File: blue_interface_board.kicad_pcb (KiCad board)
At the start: 2 copper layers, 0 parts

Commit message: Added protection from motor regeneration through capacitors + MOSFET, started placement and routing
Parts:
- added C1: 100n, Capacitor_SMD:C_0603_1608Metric, F.Cu at (96.6, 110.0)
- added C10: 27p, Capacitor_SMD:C_0603_1608Metric, F.Cu at (117.6, 120.2)
- added C11: 4.7u, Capacitor_SMD:C_0603_1608Metric, B.Cu at (113.5, 111.0)
- added C12: 100n, Capacitor_SMD:C_0603_1608Metric, B.Cu at (113.5, 112.5)
- added C13: 100n, Capacitor_SMD:C_0603_1608Metric, F.Cu at (108.8, 114.0)
- added C14: 100n, Capacitor_SMD:C_0603_1608Metric, F.Cu at (118.0, 117.0)
- added C15: 4.7u, Capacitor_SMD:C_0603_1608Metric, B.Cu at (116.5, 111.0)
- added C16: 100n, Capacitor_SMD:C_0603_1608Metric, F.Cu at (121.2, 108.5)
- added C17: 100n, Capacitor_SMD:C_0603_1608Metric, B.Cu at (116.5, 112.5)
- added C18: 100n, Capacitor_SMD:C_0603_1608Metric, F.Cu at (124.8, 108.1)
- added C19: 10n, Capacitor_SMD:C_0603_1608Metric, F.Cu at (126.2, 108.1)
- added C2: 4.7u, Capacitor_SMD:C_0603_1608Metric, F.Cu at (107.5, 108.0)
- added C20: 100n, Capacitor_SMD:C_0603_1608Metric, F.Cu at (126.2, 115.8)
- added C21: 10u, Capacitor_SMD:C_0603_1608Metric, F.Cu at (124.8, 115.8)
- added C22: 100n, Capacitor_SMD:C_0603_1608Metric, F.Cu at (142.0, 108.2)
- added C23: 10n, Capacitor_SMD:C_0603_1608Metric, F.Cu at (140.5, 108.2)
- added C24: 100n, Capacitor_SMD:C_0603_1608Metric, F.Cu at (140.5, 115.8)
- added C25: 10u, Capacitor_SMD:C_0603_1608Metric, F.Cu at (142.0, 115.8)
- added C26: 10n, Capacitor_SMD:C_0603_1608Metric, F.Cu at (101.2, 115.0)
- added C27: 150nF, Capacitor_SMD:C_1206_3216Metric, F.Cu at (67.7, 77.5)
- added C28: 100nF, Capacitor_SMD:C_1206_3216Metric, F.Cu at (-96.5, 58.5)
- added C29: 1uF, Capacitor_SMD:C_0603_1608Metric, F.Cu at (87.1, 65.8)
- added C3: 4.7u, Capacitor_SMD:C_0603_1608Metric, B.Cu at (107.5, 108.0)
- added C30: 1uF, Capacitor_SMD:C_0603_1608Metric, F.Cu at (82.6, 70.4)
- added C31: 100n, Capacitor_SMD:C_0603_1608Metric, F.Cu at (113.2, 40.7)
- added C32: 470u, Capacitor_SMD:CP_Elec_18x17.5, F.Cu at (-49.0, 46.0)
- added C33: 470u, Capacitor_SMD:CP_Elec_18x17.5, F.Cu at (-29.0, 46.0)
- added C34: 470u, Capacitor_SMD:CP_Elec_18x17.5, F.Cu at (11.0, 46.0)
- added C35: 470u, Capacitor_SMD:CP_Elec_18x17.5, F.Cu at (-9.00, 46.0)
- added C38: 1u, Capacitor_SMD:C_0603_1608Metric, F.Cu at (47.0, 78.2)
- added C39: 1u, Capacitor_SMD:C_0603_1608Metric, F.Cu at (26.9, 78.2)
- added C4: 100n, Capacitor_SMD:C_0603_1608Metric, B.Cu at (112.8, 107.0)
- added C40: 100n, Capacitor_SMD:C_0603_1608Metric, F.Cu at (-84.0, 40.0)
- added C5: 10n, Capacitor_SMD:C_0603_1608Metric, F.Cu at (114.0, 104.2)
- added C6: 100n, Capacitor_SMD:C_0603_1608Metric, F.Cu at (109.0, 108.0)
- added C7: 100n, Capacitor_SMD:C_0603_1608Metric, B.Cu at (109.0, 108.0)
- added C8: 100n, Capacitor_SMD:C_0603_1608Metric, F.Cu at (110.5, 106.0)
- added C9: 27p, Capacitor_SMD:C_0603_1608Metric, F.Cu at (107.4, 120.2)
- added D1: LED, LED_SMD:LED_0603_1608Metric, F.Cu at (118.5, 99.8)
- added D2: LED, LED_SMD:LED_0603_1608Metric, F.Cu at (116.6, 99.8)
- added D3: 1N4148W-7-F, Diode_SMD:D_SOD-123, F.Cu at (67.8, 74.2)
- added D4: 5.0SMDJ51A, Diode_SMD:D_SMC, F.Cu at (-103.0, 58.5)
- added D5: B380-13-F, Diode_SMD:D_SMC, F.Cu at (-63.5, 56.5)
- added D6: LED, LED_SMD:LED_0603_1608Metric, F.Cu at (22.9, 78.2)
- added FB1: 600R, Resistor_SMD:R_0603_1608Metric, B.Cu at (113.5, 109.5)
- added FB2: 600R, Resistor_SMD:R_0603_1608Metric, B.Cu at (116.5, 109.5)
- added FB3: 600R, Resistor_SMD:R_0603_1608Metric, F.Cu at (103.0, 115.0)
- added J1: Conn_01x05, Connector_Molex:Molex_Micro-Fit_3.0_43650-0500_1x05_P3.00mm_Horizontal, F.Cu at (149.2, 97.5)
- added J2: USB_B_Micro, Connector_USB:USB_Micro-B_Wuerth_629105150521_CircularHoles, F.Cu at (96.2, 118.5)
- added J3: Conn_01x02, Connector_Molex:Molex_Nano-Fit_105313-xx02_1x02_P2.50mm_Horizontal, F.Cu at (58.4, 67.3)
- added J4: Conn_01x02, Connector_PinHeader_2.54mm:PinHeader_1x02_P2.54mm_Horizontal, F.Cu at (-109.5, 59.5)
- added Q1: MMBT5401LT1G, Package_TO_SOT_SMD:SOT-23, F.Cu at (82.8, 66.8)
- added Q2: Q_NMOS_GDS, Package_TO_SOT_SMD:TO-263-2, F.Cu at (-79.0, 60.5)
- added Q3: MMBT3904, Package_TO_SOT_SMD:SOT-23, F.Cu at (78.5, 74.6)
- added Q4: Q_NMOS_GDS, Package_TO_SOT_SMD:SOT-23, F.Cu at (109.0, 41.7)
- added Q5: Q_NMOS_GDS, Package_TO_SOT_SMD:TO-263-2, F.Cu at (-68.0, 37.5)
- added R1: 10K, Resistor_SMD:R_0603_1608Metric, F.Cu at (106.0, 113.2)
- added R10: 140k, Resistor_SMD:R_0603_1608Metric, F.Cu at (34.9, 78.2)
- added R11: 6.65k, Resistor_SMD:R_0603_1608Metric, F.Cu at (38.9, 78.2)
- added R12: 150k, Resistor_SMD:R_0603_1608Metric, F.Cu at (42.9, 78.2)
- added R13: 25.5k, Resistor_SMD:R_0603_1608Metric, F.Cu at (82.7, 75.4)
- added R14: 2m, Resistor_SMD:R_2512_6332Metric, F.Cu at (-90.0, 57.0)
- added R15: 240k, Resistor_SMD:R_0603_1608Metric, F.Cu at (51.0, 78.2)
- added R16: 13.3k, Resistor_SMD:R_0603_1608Metric, F.Cu at (111.8, 45.7)
- added R17: 47k, Resistor_SMD:R_0603_1608Metric, F.Cu at (96.6, 60.2)
- added R18: 100k, Resistor_SMD:R_0603_1608Metric, F.Cu at (91.1, 65.8)
- added R19: 1M, Resistor_SMD:R_0603_1608Metric, F.Cu at (113.2, 43.2)
- added R2: 10K, Resistor_SMD:R_0603_1608Metric, F.Cu at (104.0, 105.8)
- added R20: 220R, Resistor_SMD:R_0603_1608Metric, F.Cu at (107.4, 49.5)
- added R21: 10R, Package_TO_SOT_THT:TO-247-2_Vertical, F.Cu at (25.5, 51.5)
- added R22: 100k, Resistor_SMD:R_0603_1608Metric, F.Cu at (82.7, 72.9)
- added R23: 49.9k, Resistor_SMD:R_0603_1608Metric, F.Cu at (101.0, 54.3)
- added R24: 2.7k, Resistor_SMD:R_0603_1608Metric, F.Cu at (87.1, 68.3)
- added R25: 82.5k, Resistor_SMD:R_0805_2012Metric, F.Cu at (-70.0, 52.0)
- added R26: 24.9k, Resistor_SMD:R_0805_2012Metric, F.Cu at (-70.0, 48.0)
- added R27: 75k, Resistor_SMD:R_0805_2012Metric, F.Cu at (-93.0, 50.5)
- added R28: 24.9k, Resistor_SMD:R_0805_2012Metric, F.Cu at (-93.0, 46.5)
- added R29: 2M, Resistor_SMD:R_0603_1608Metric, F.Cu at (76.9, 78.1)
- added R3: 2k, Resistor_SMD:R_0603_1608Metric, F.Cu at (106.0, 109.0)
- added R4: 10K, Resistor_SMD:R_0603_1608Metric, F.Cu at (102.5, 105.8)
- added R5: 10K, Resistor_SMD:R_0603_1608Metric, F.Cu at (114.0, 102.6)
- added R6: 12K, Resistor_SMD:R_0603_1608Metric, F.Cu at (118.0, 118.5)
- added R7: 220R, Resistor_SMD:R_0603_1608Metric, F.Cu at (118.5, 103.0)
- added R8: 220R, Resistor_SMD:R_0603_1608Metric, F.Cu at (116.6, 103.0)
- added R9: 1k, Resistor_SMD:R_0603_1608Metric, F.Cu at (30.9, 78.2)
- added U1: 93LCxxB, Package_SO:SOIC-8_3.9x4.9mm_P1.27mm, F.Cu at (101.5, 110.2)
- added U2: FT232H, Package_QFP:LQFP-48_7x7mm_P0.5mm, F.Cu at (115.0, 111.0)
- added U3: ADM2682E, Package_SO:SOIC-16W_7.5x12.8mm_P1.27mm, F.Cu at (133.2, 112.0)
- added U4: TPD2E2U06, Package_TO_SOT_SMD:SOT-553, F.Cu at (146.2, 112.0)
- added U5: TPD2E2U06, Package_TO_SOT_SMD:SOT-553, F.Cu at (101.7, 118.2)
- added U6: LM5066, TI:Texas_PWP0028A, F.Cu at (113.5, 34.8)
- added U7: LM311, Package_SO:SOIC-8_3.9x4.9mm_P1.27mm, F.Cu at (-81.0, 45.0)
- added U8: LR8K4-G, Package_TO_SOT_SMD:TO-252-2, F.Cu at (100.7, 41.3)
- added Y1: 12MHz, Crystal:Crystal_SMD_5032-2Pin_5.0x3.2mm, F.Cu at (112.5, 119.8)
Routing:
- net GNDD: track 0.00 -> 61.8 mm, vias 0 -> 18
- net +3V3: track 0.00 -> 42.6 mm, vias 0 -> 13
- net /Comms/DP: track 0.00 -> 20.3 mm, vias 0 -> 2
- net /Comms/DN: track 0.00 -> 19.6 mm, vias 0 -> 2
- net GNDPWR: track 0.00 -> 19.0 mm, vias 0 -> 6
- net Net-(R27-Pad2): track 0.00 -> 17.5 mm
- net Net-(R25-Pad2): track 0.00 -> 16.6 mm
- net /Comms/VISO: track 0.00 -> 14.3 mm, vias 0 -> 2
- net +5V: track 0.00 -> 13.7 mm, vias 0 -> 2
- net /Comms/EECLK: track 0.00 -> 12.8 mm
- net Net-(Q5-Pad1): track 0.00 -> 12.1 mm
- net /Comms/RS485_DE: track 0.00 -> 11.4 mm, vias 0 -> 2
- net /Comms/RS485_RX: track 0.00 -> 10.8 mm
- net /Comms/RS485_TX: track 0.00 -> 9.50 mm
- net Net-(C10-Pad1): track 0.00 -> 7.94 mm
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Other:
- net class Default: clearance 0.2 -> 0.2032; trace_width 0.25 -> 0.3048; via_dia 0.8 -> 0.762; via_drill 0.4 -> 0.381
- rule trace_clearance: 0.2 -> 0.2032
- rule trace_min: 0.2 -> 0.1778

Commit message: WIP with component placement
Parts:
- removed C40: 100n, Capacitor_SMD:C_0603_1608Metric
- removed R29: 2M, Resistor_SMD:R_0603_1608Metric
- added C36: 1nF, Capacitor_SMD:C_0603_1608Metric, F.Cu at (128.8, 82.6)
- added J5: Conn_ARM_JTAG_SWD_10, Connector_PinHeader_1.27mm:PinHeader_2x05_P1.27mm_Vertical, F.Cu at (87.8, 76.0)
- C11, C12, C15, C17, C3, C4, C7, FB1, FB2: moved to F.Cu
- C33, C34, C35: value 470u -> 100n; footprint Capacitor_SMD:CP_Elec_18x17.5 -> Capacitor_SMD:C_0603_1608Metric
- C38: footprint Capacitor_SMD:C_0603_1608Metric -> Capacitor_SMD:C_1206_3216Metric
- C39: footprint Capacitor_SMD:C_0603_1608Metric -> Capacitor_SMD:C_0805_2012Metric
- J4: footprint Connector_PinHeader_2.54mm:PinHeader_1x02_P2.54mm_Horizontal -> Connectors_OSRF:PP45_1X2
- R23: value 49.9k -> 18.2K
- R24: value 2.7k -> 11.5K
- R25: value 82.5k -> 82.9k
- U7: value LM311 -> STM32L011K4Tx; footprint Package_SO:SOIC-8_3.9x4.9mm_P1.27mm -> Package_QFP:LQFP-32_7x7mm_P0.8mm
- moved R27 204.1 mm to (110.1, 70.4), turned to 180 degrees
- moved C28 201.0 mm to (101.5, 93.0)
- moved D5 199.2 mm to (133.0, 89.0)
- moved R28 197.9 mm to (103.6, 69.4)
- moved Q2 194.2 mm to (114.3, 79.1), turned to 180 degrees
- moved R14 192.2 mm to (101.0, 78.0)
- moved J4 187.9 mm to (76.2, 88.0), turned to 0 degrees
- moved C32 186.0 mm to (135.4, 70.6), turned to 0 degrees
- moved Q5 183.1 mm to (113.4, 62.9)
- moved D4 180.8 mm to (76.2, 81.8), turned to 180 degrees
- moved U7 176.2 mm to (94.3, 62.2)
- moved R26 174.9 mm to (103.0, 73.5), turned to 0 degrees
- moved R25 170.9 mm to (99.5, 73.5), turned to 0 degrees
- moved C33 124.9 mm to (93.8, 68.8), turned to 180 degrees
- moved D6 106.0 mm to (127.3, 96.6), turned to 180 degrees
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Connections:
- C32 pad 2: /Power/PROT_DRAIN -> GNDPWR
- C33 pad 1: VOUT -> +3.3VP
- C33 pad 2: /Power/PROT_DRAIN -> GNDPWR
- C34 pad 1: VOUT -> +3.3VP
- C34 pad 2: /Power/PROT_DRAIN -> GNDPWR
- C35 pad 1: VOUT -> +3.3VP
- C35 pad 2: /Power/PROT_DRAIN -> GNDPWR
- C39 pad 1: +24V -> +3.3VP
- J4 pad 1: GNDPWR -> /Power/VIN
- J4 pad 2: /Power/VIN -> GNDPWR
- Q5 pad 2: /Power/PROT_DRAIN -> Net-(Q5-Pad2)
- R13 pad 2: Net-(R13-Pad2) -> GNDPWR
- R15 pad 2: Net-(R15-Pad2) -> VOUT
- R21 pad 1: VOUT -> Net-(Q5-Pad2)
- R21 pad 2: /Power/PROT_DRAIN -> VOUT
- R24 pad 1: +24V -> +3.3VP
- R25 pad 1: VOUT -> /Power/VIN
- R27 pad 1: /Power/VIN -> VOUT
- U7 pad 1: GNDPWR -> +3.3VP
- U7 pad 2: Net-(R25-Pad2) -> Net-(U7-Pad2)
- U7 pad 3: Net-(R27-Pad2) -> Net-(U7-Pad3)
- U7 pad 4: GNDPWR -> /Power/nRST
- U7 pad 5: Net-(U7-Pad5) -> +3.3VP
- U7 pad 6: Net-(U7-Pad6) -> Net-(R25-Pad2)
- U7 pad 7: Net-(Q5-Pad1) -> Net-(R27-Pad2)
- U7 pad 8: +24V -> Net-(R27-Pad2)
- U8 pad 2: +24V -> +3.3VP
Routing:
- net Net-(J3-Pad2): track 0.00 -> 51.5 mm, vias 0 -> 2
- net GNDD: track 61.8 -> 30.0 mm, vias 18 -> 8
- net /Power/GATE: track 0.00 -> 25.2 mm
- net VOUT: track 6.57 -> 31.3 mm
- net Net-(R10-Pad2): track 0.00 -> 17.6 mm, vias 0 -> 2
- net Net-(R27-Pad2): track 17.5 -> 0.00 mm
- net Net-(R25-Pad2): track 16.6 -> 0.00 mm
- net Net-(Q5-Pad1): track 12.1 -> 0.00 mm
- net +3V3: track 42.6 -> 32.4 mm, vias 13 -> 8
- net +5V: track 13.7 -> 3.78 mm, vias 2 -> 1
- net GNDPWR: track 19.0 -> 9.82 mm, vias 6 -> 1
- net /Comms/DN: track 19.6 -> 25.6 mm
- net /Power/VIN: track 5.06 -> 0.00 mm
- net Net-(R7-Pad2): track 3.77 -> 0.00 mm
- net /Comms/DP: track 20.3 -> 23.7 mm
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
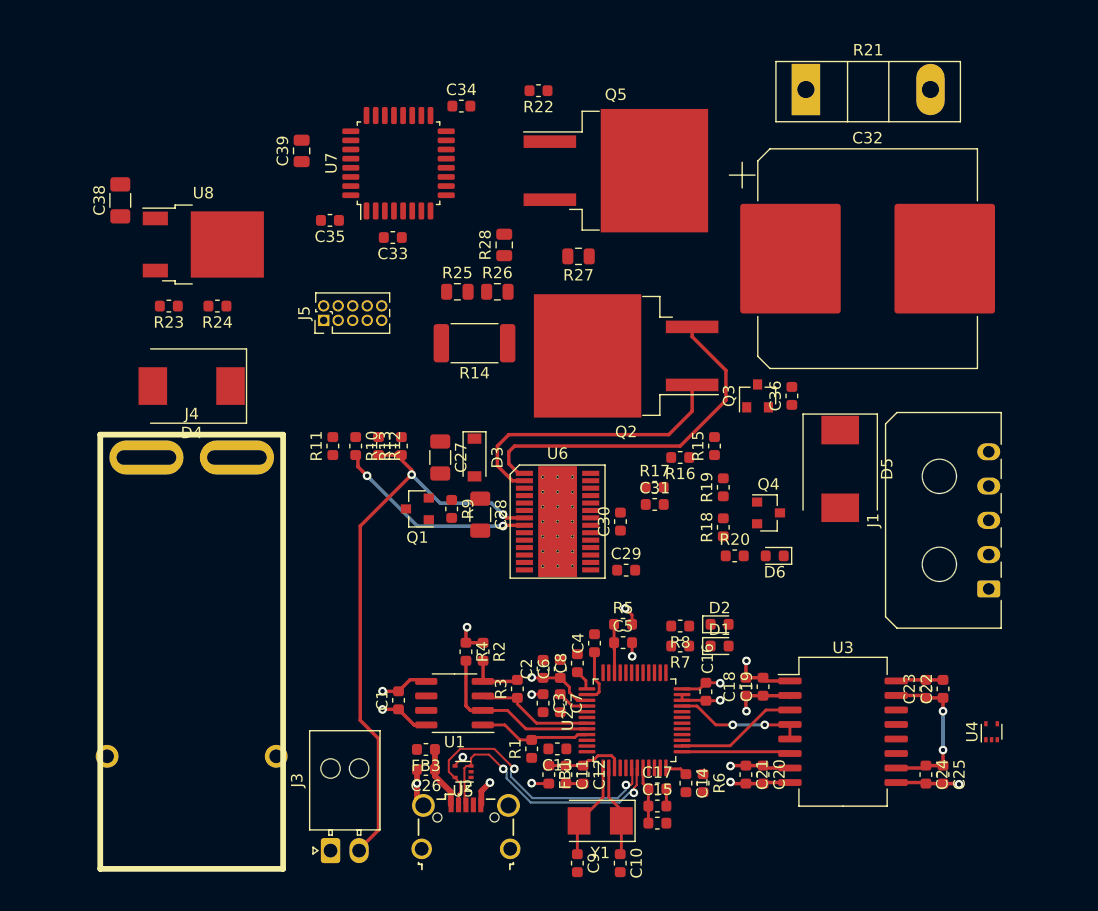
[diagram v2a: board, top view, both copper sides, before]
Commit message: Finished schematic, placement and routing, only silkscreen TODO
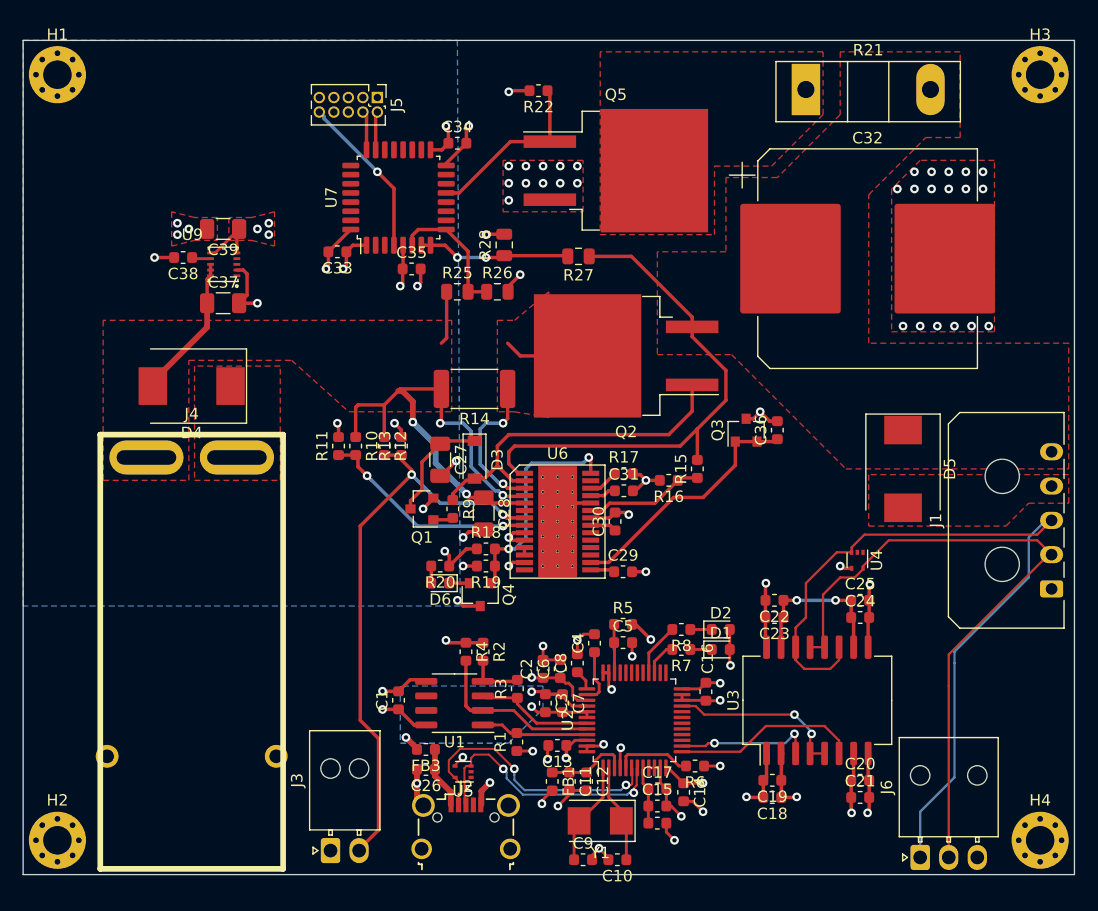
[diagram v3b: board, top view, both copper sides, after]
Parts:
- removed R23: 18.2K, Resistor_SMD:R_0603_1608Metric
- removed R24: 11.5K, Resistor_SMD:R_0603_1608Metric
- removed U8: LR8K4-G, Package_TO_SOT_SMD:TO-252-2
- added C37: 1u, Capacitor_SMD:C_1206_3216Metric, F.Cu at (79.0, 74.5)
- added H1: MountingHole, MountingHole:MountingHole_2.5mm_Pad_Via, F.Cu at (64.5, 54.5)
- added H2: MountingHole, MountingHole:MountingHole_2.5mm_Pad_Via, F.Cu at (64.5, 121.5)
- added H3: MountingHole, MountingHole:MountingHole_2.5mm_Pad_Via, F.Cu at (150.5, 54.5)
- added H4: MountingHole, MountingHole:MountingHole_2.5mm_Pad_Via, F.Cu at (150.5, 121.5)
- added J6: Conn_01x03, Connector_Molex:Molex_Nano-Fit_105313-xx03_1x03_P2.50mm_Horizontal, F.Cu at (140.0, 123.0)
- added U9: MAXM15062, DCDC:MAXIM_uSLIP-10, F.Cu at (79.0, 71.0)
- C38: footprint Capacitor_SMD:C_1206_3216Metric -> Capacitor_SMD:C_0603_1608Metric
- C39: value 1u -> 10u; footprint Capacitor_SMD:C_0805_2012Metric -> Capacitor_SMD:C_1206_3216Metric
- moved D6 29.4 mm to (98.0, 99.0)
- moved Q4 26.2 mm to (101.5, 100.0), turned to 270 degrees
- moved R20 25.8 mm to (98.0, 97.5), turned to 180 degrees
- moved R19 21.9 mm to (102.0, 97.5), turned to 180 degrees
- moved R18 20.9 mm to (102.0, 96.0), turned to 0 degrees
- moved J5 20.1 mm to (92.5, 56.5), turned to 270 degrees
- moved U4 19.1 mm to (134.5, 97.0), turned to 270 degrees
- moved C25 16.9 mm to (134.8, 100.5), turned to 0 degrees
- moved C22 16.7 mm to (127.2, 100.5), turned to 180 degrees
- moved C24 14.9 mm to (134.8, 102.0), turned to 0 degrees
- moved C23 14.7 mm to (127.2, 102.0), turned to 180 degrees
- moved C21 10.2 mm to (134.8, 117.8), turned to 0 degrees
- moved C18 9.96 mm to (127.1, 117.8), turned to 180 degrees
- moved C39 9.69 mm to (79.0, 68.0), turned to 180 degrees
- moved C20 8.51 mm to (134.8, 116.2), turned to 0 degrees
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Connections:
- C30 pad 1: /Power/LM_VDD -> Net-(C30-Pad1)
- C38 pad 1: /Power/VIN -> Net-(C38-Pad1)
- R18 pad 1: /Power/LM_VDD -> +3.3VP
- R20 pad 1: /Power/LM_VDD -> +3.3VP
- U6 pad 21: /Power/LM_VDD -> Net-(C30-Pad1)
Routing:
- net /Comms/RS485_A: track 0.00 -> 71.3 mm
- net /Power/VIN: track 0.00 -> 62.8 mm, vias 0 -> 4
- net /Comms/RS485_B: track 0.00 -> 58.5 mm
- net GNDPWR: track 9.82 -> 66.5 mm, vias 1 -> 55
- net GNDD: track 30.0 -> 60.6 mm, vias 8 -> 20
- net Net-(C36-Pad1): track 0.00 -> 22.0 mm
- net +3.3VP: track 0.00 -> 21.2 mm, vias 0 -> 7
- net Net-(Q2-Pad2): track 0.00 -> 20.7 mm, vias 0 -> 2
- net /Power/PGD: track 0.00 -> 19.6 mm, vias 0 -> 2
- net Net-(Q5-Pad1): track 0.00 -> 15.5 mm
- net VOUT: track 31.3 -> 46.3 mm
- net /Power/nRST: track 0.00 -> 14.4 mm, vias 0 -> 1
- net Net-(R27-Pad2): track 0.00 -> 13.4 mm, vias 0 -> 2
- net +3V3: track 32.4 -> 45.1 mm, vias 8 -> 13
- net Net-(R25-Pad2): track 0.00 -> 11.9 mm
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- added copper zone on B.Cu, net +3.3VP
- added copper zone on F.Cu, net +3.3VP
- added copper zone on In1.Cu, net +3V3
- added copper zone on B.Cu, net +5V
- added copper zone on F.Cu, net /Power/VIN
- added copper zone on In2.Cu, net GNDD
- added copper zone on F.Cu, net GNDPWR
- added copper zone on In1.Cu, net GNDPWR
- added copper zone on In2.Cu, net GNDPWR
- added copper zone on F.Cu, net Net-(Q2-Pad2)
- added copper zone on F.Cu, net Net-(Q5-Pad2)
- added copper zone on F.Cu, net VOUT
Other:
- board outline added: 92 x 73 mm
- copper layers 2 -> 4
- net class Default: clearance 0.2032 -> 0.1524
- rule trace_clearance: 0.2032 -> 0.1524
